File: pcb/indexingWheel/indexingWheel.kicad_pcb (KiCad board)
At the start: 2 copper layers, 43 x 43 mm, 6 parts

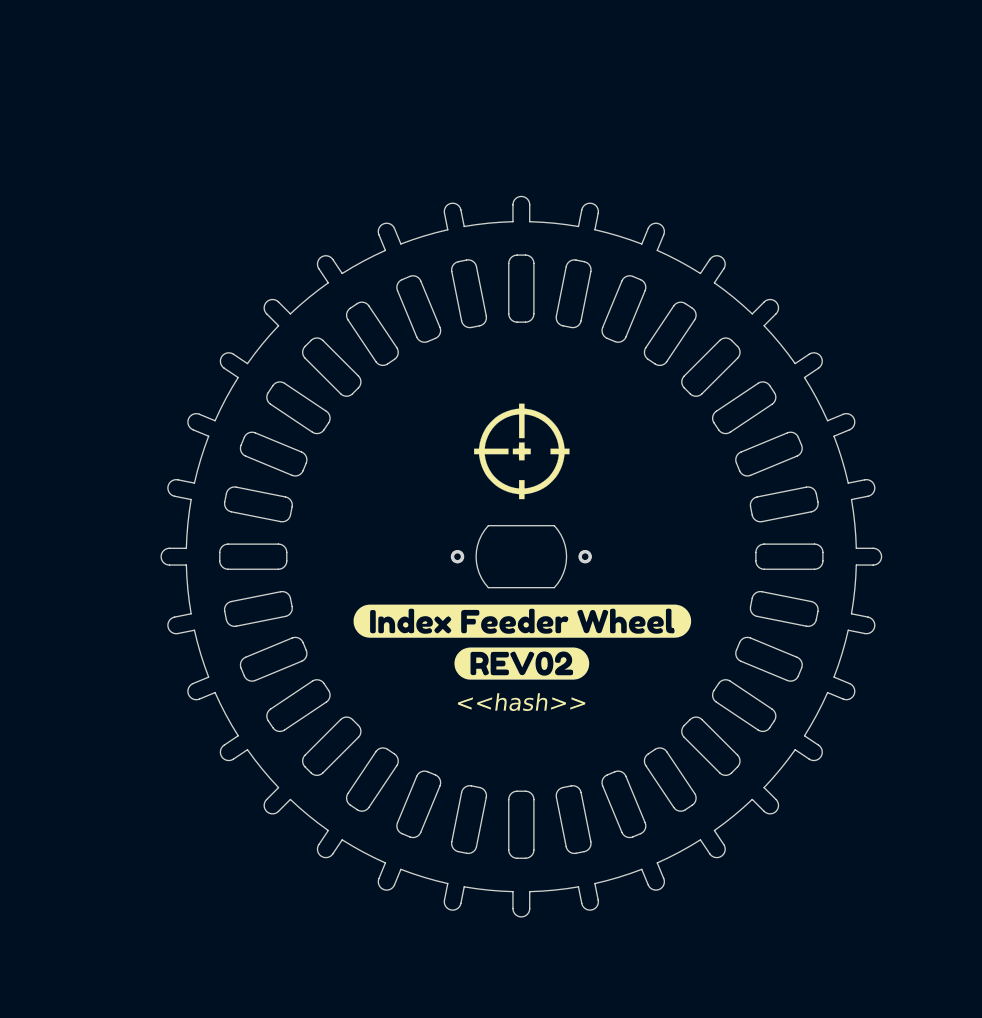
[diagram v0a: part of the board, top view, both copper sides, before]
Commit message: represents rev07 feeder controller, rev03 indexing wheel, rev03 feeder floor. also checks in lots of cad work for feeder design and feeder floor design
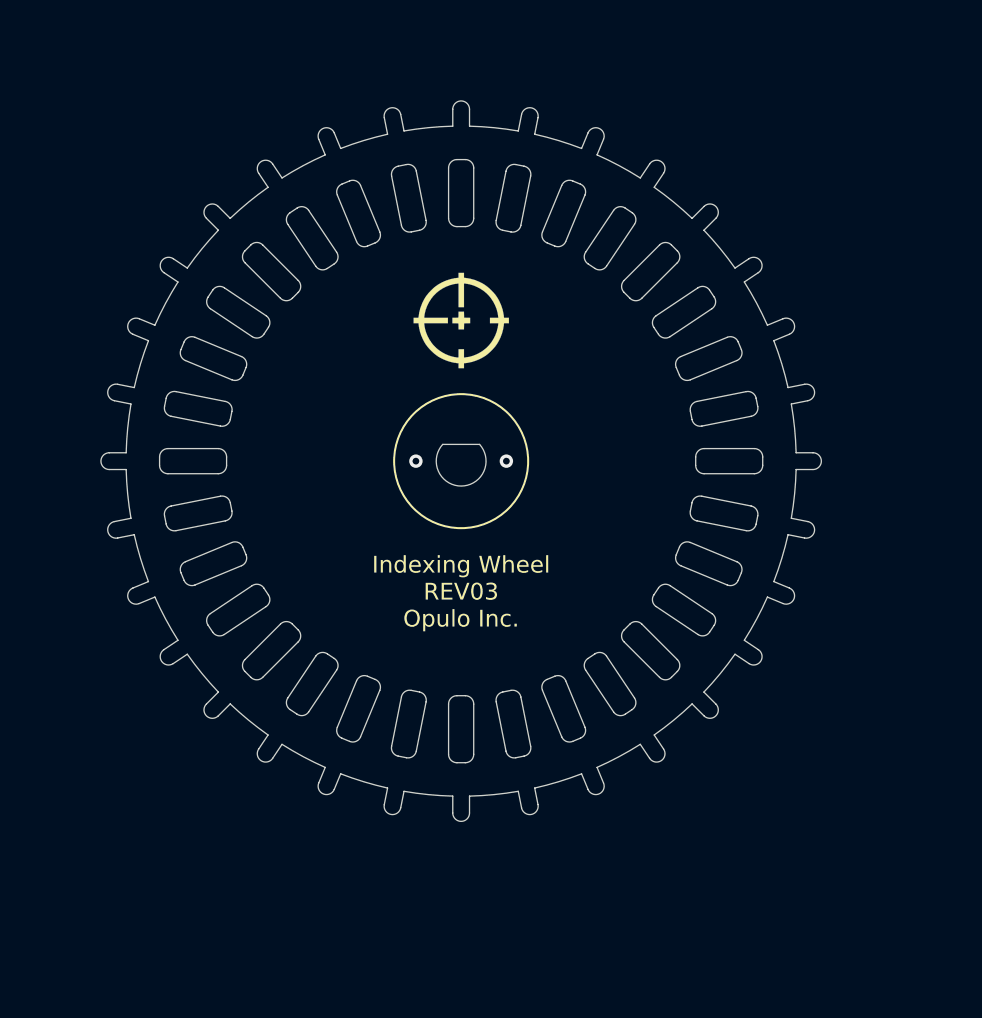
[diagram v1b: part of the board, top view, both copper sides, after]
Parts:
- removed svg2mod (x4): G***, label
- moved G*** 8.62 mm to (149.5, 84.6)
- moved G*** 8.61 mm to (149.5, 84.6)
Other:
- outline, holes or cut-outs redrawn
- board text added: "Indexing Wheel REV03 Opulo Inc."
- board text removed: "<<hash>>"

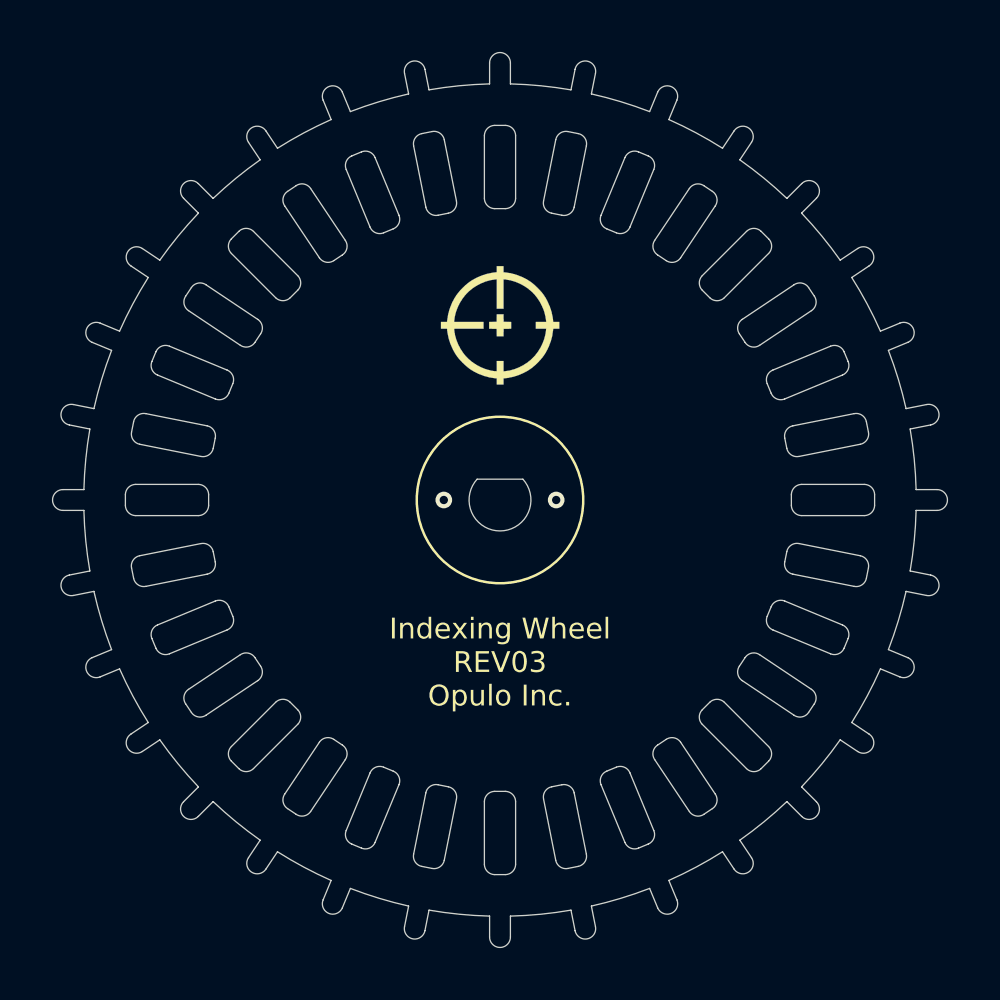
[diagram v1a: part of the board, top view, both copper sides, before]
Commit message: this commit represents rev09 of the controller, rev04 of the indexing wheel, and rev05 of the feeder floor
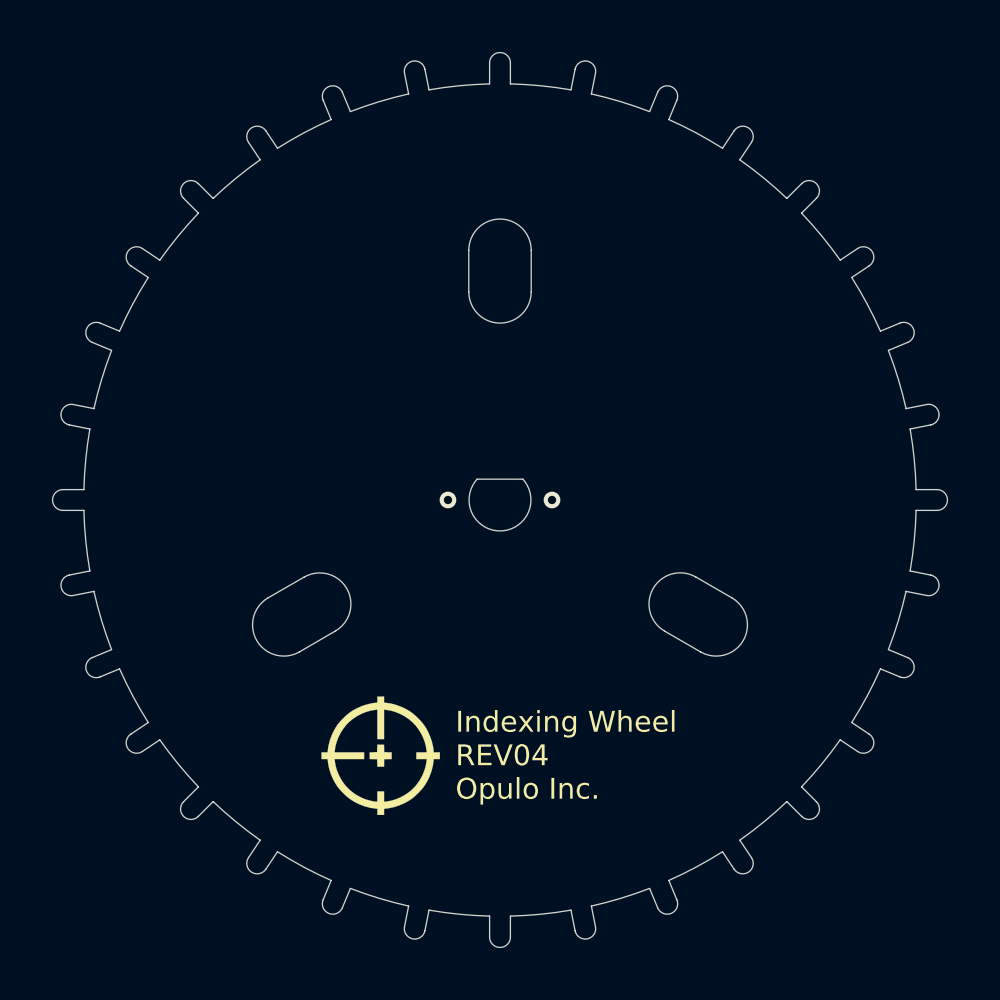
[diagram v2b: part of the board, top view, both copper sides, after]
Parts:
- removed the G*** at (149.5, 84.6)
- moved G*** 21.5 mm to (143.8, 105.3)
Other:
- outline, holes or cut-outs redrawn
- board text added: "Indexing Wheel REV04 Opulo Inc."
- board text removed: "Indexing Wheel REV03 Opulo Inc."

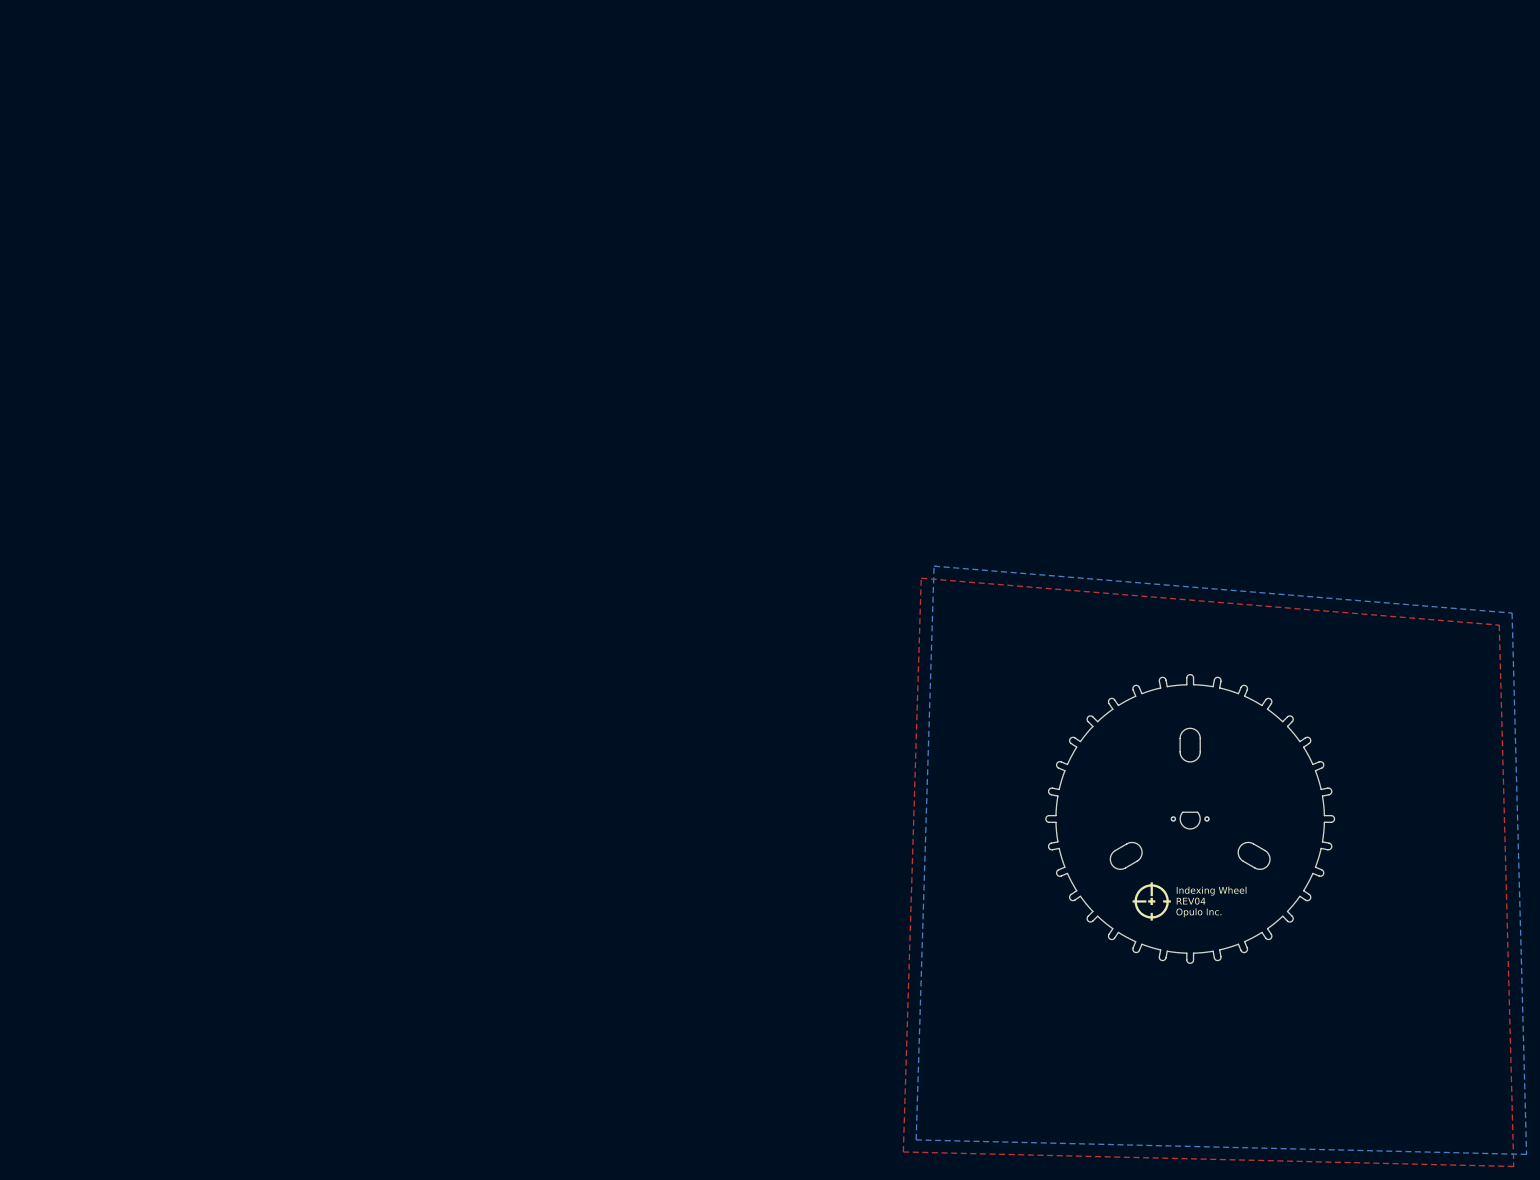
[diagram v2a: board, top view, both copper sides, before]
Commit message: adds dogbone cutouts to indexing wheel for better positioning, more alignment features, holes for potential screw-mounted shaft collars
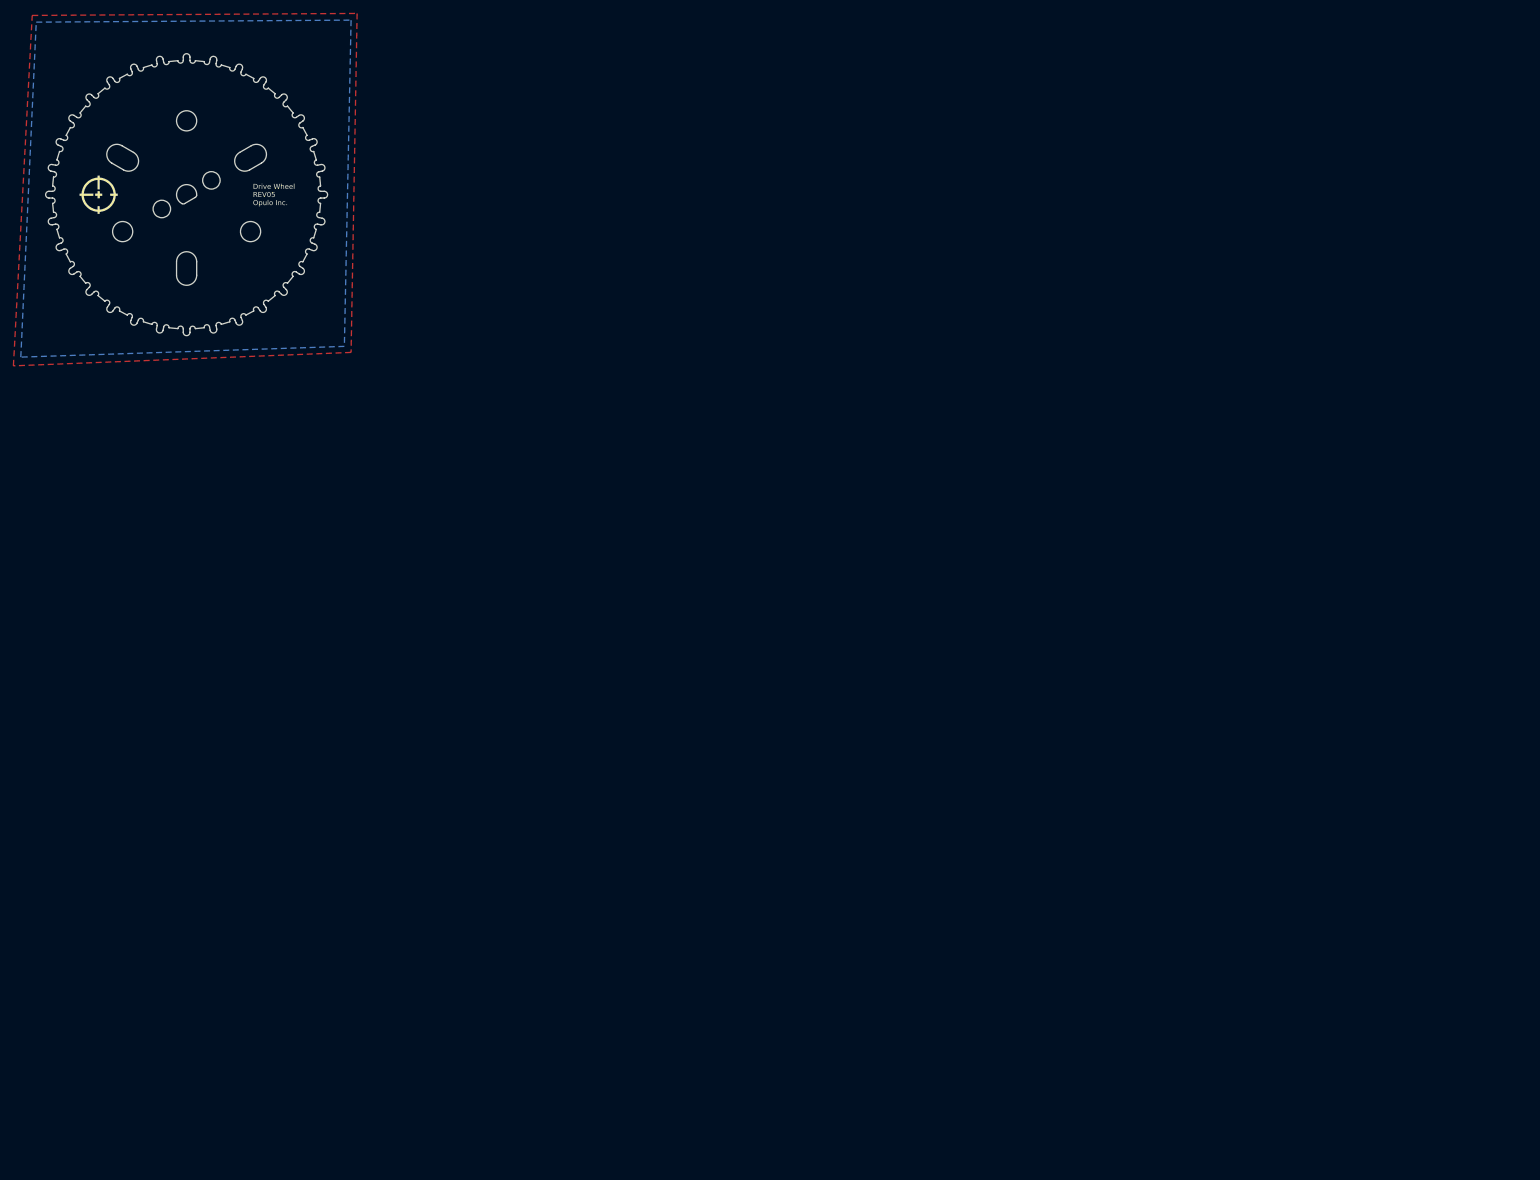
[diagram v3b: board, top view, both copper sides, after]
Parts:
- moved G*** 188.9 mm to (-13.1, 0.00)
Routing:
- net (no net): vias 2 -> 0
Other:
- board size 43 x 43 mm -> 42 x 42 mm
- board text added: "Drive Wheel REV05 Opulo Inc."
- board text removed: "Indexing Wheel REV04 Opulo Inc."

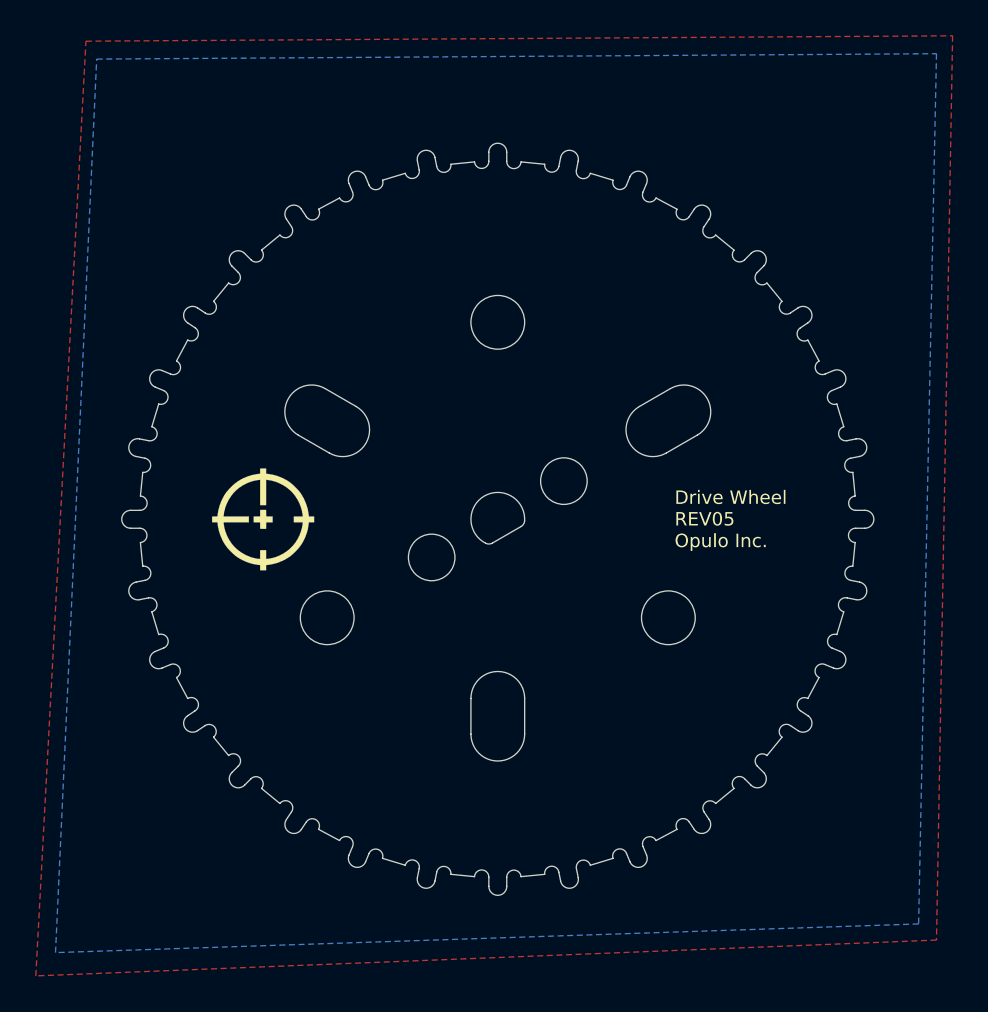
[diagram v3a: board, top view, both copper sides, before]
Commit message: updates indexing wheel to rev06
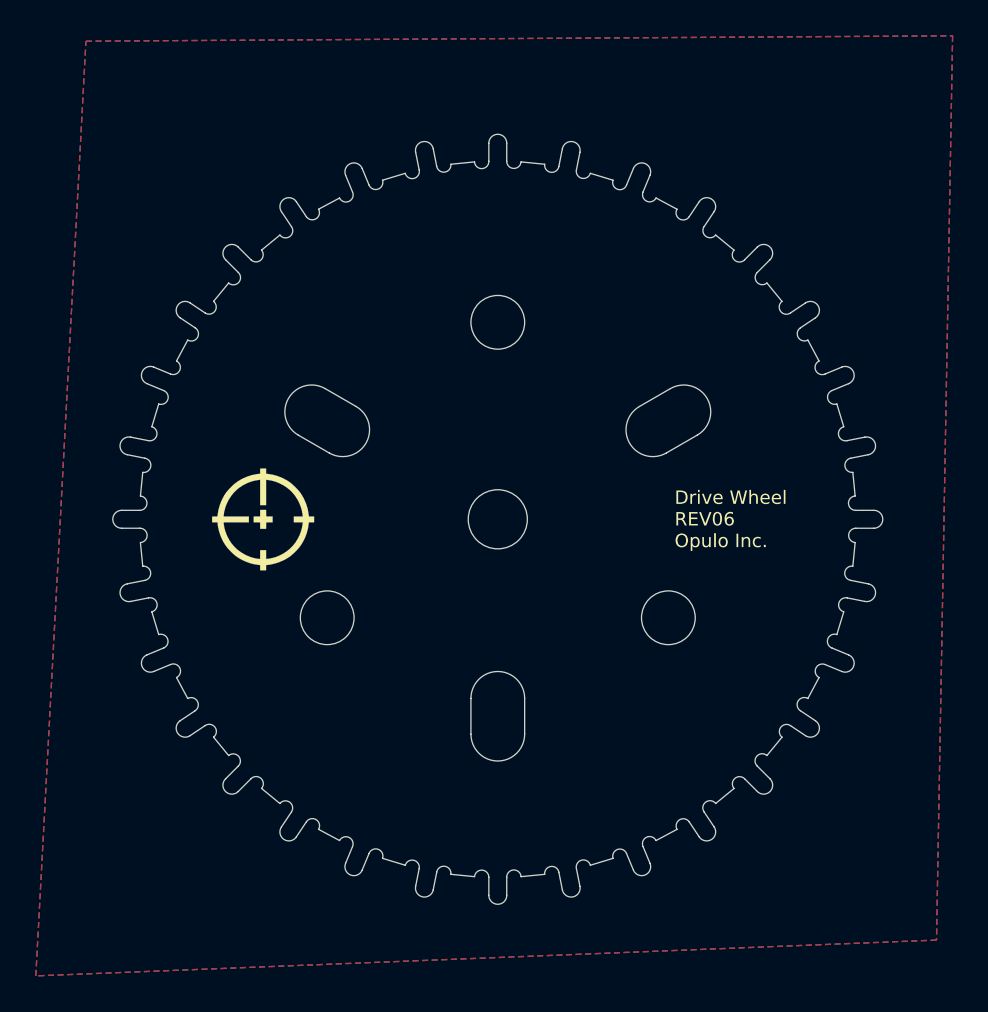
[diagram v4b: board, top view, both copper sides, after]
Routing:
- added copper zone on B.Cu, net GND
- added copper zone on F.Cu, net GND
- removed copper zone on B.Cu, net (none)
- removed copper zone on F.Cu, net (none)
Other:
- board size 42 x 42 mm -> 43 x 43 mm
- board text added: "Drive Wheel REV06 Opulo Inc."
- board text removed: "Drive Wheel REV05 Opulo Inc."
